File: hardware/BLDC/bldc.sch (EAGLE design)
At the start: 87 parts, among them J1 PWR_2_XT30PW-M, J2 LINEAR_3_JST_PH_RA, J3 LINEAR_8_JST_PH_RA, U1 MA702, U10 MCP2542FD, U11 LDFM33PUR, U2 DRV8323RS, U3 TPN7R006PL, U4 TPN7R006PL, U5 TPN7R006PL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

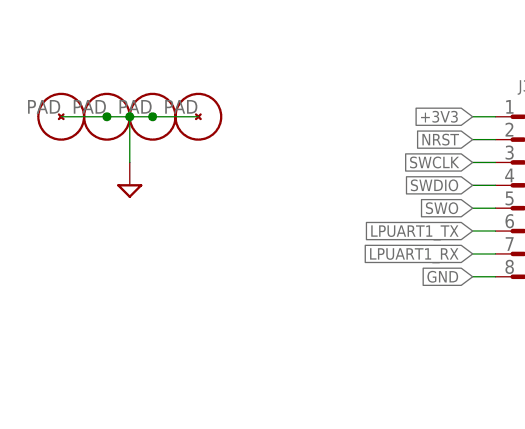
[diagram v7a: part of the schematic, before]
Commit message: Eagle board thickness
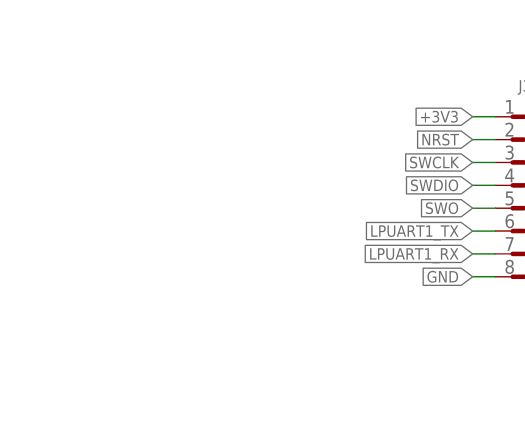
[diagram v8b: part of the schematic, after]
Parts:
- removed H1, H2, H3, H4: PCB_MOUNT_HOLE_M2, _T_conn:PCB_MOUNT_HOLE_M2
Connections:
- net GND: no longer H1.P1, H2.P1, H3.P1, H4.P1
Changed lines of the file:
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@@
 <schematic_group name="FDCAN"/>
 <schematic_group name="POWER_CONN"/>
-<schematic_group name="MOUNTING_HOLES"/>
 <schematic_group name="5V_3.3V_REG"/>
 <schematic_group name="LED_INFO"/>
@@
 <part name="U7" library="_T_transistors" library_urn="urn:adsk.eagle:library:19605452" deviceset="TPN7R006PL" device="" package3d_urn="urn:adsk.eagle:package:20292156/4"/>
 <part name="U8" library="_T_transistors" library_urn="urn:adsk.eagle:library:19605452" deviceset="TPN7R006PL" device="" package3d_urn="urn:adsk.eagle:package:20292156/4"/>
-<part name="H1" library="_T_conn" library_urn="urn:adsk.eagle:library:19570503" deviceset="PCB_MOUNT_HOLE" device="_M2" package3d_urn="urn:adsk.eagle:package:20293119/4"/>
-<part name="H2" library="_T_conn" library_urn="urn:adsk.eagle:library:19570503" deviceset="PCB_MOUNT_HOLE" device="_M2" package3d_urn="urn:adsk.eagle:package:20293119/4"/>
-<part name="H3" library="_T_conn" library_urn="urn:adsk.eagle:library:19570503" deviceset="PCB_MOUNT_HOLE" device="_M2" package3d_urn="urn:adsk.eagle:package:20293119/4"/>
-<part name="H4" library="_T_conn" library_urn="urn:adsk.eagle:library:19570503" deviceset="PCB_MOUNT_HOLE" device="_M2" package3d_urn="urn:adsk.eagle:package:20293119/4"/>
-<part name="GND2" library="_T_power" library_urn="urn:adsk.eagle:library:19572085" deviceset="GND" device=""/>
 <part name="U9" library="_T_ic" library_urn="urn:adsk.eagle:library:19571245" deviceset="STM32G4_UFQFPN48_T1" device="" package3d_urn="urn:adsk.eagle:package:19324073/6"/>
 <part name="L1" library="_T_rcl" library_urn="urn:adsk.eagle:library:19571919" deviceset="DC_CHOKE" device="_FERRITE_BEAD_0603" package3d_urn="urn:adsk.eagle:package:20293176/3" value="600R@100MHz"/>
@@
 <attribute name="NAME" x="250.19" y="90.17" size="1.27" layer="95" rot="MR180"/>
 </instance>
-<instance part="H1" gate="G$1" x="-83.82" y="175.26" smashed="yes" grouprefs="MOUNTING_HOLES"/>
-<instance part="H2" gate="G$1" x="-78.74" y="175.26" smashed="yes" grouprefs="MOUNTING_HOLES"/>
-<instance part="H3" gate="G$1" x="-73.66" y="175.26" smashed="yes" grouprefs="MOUNTING_HOLES"/>
-<instance part="H4" gate="G$1" x="-68.58" y="175.26" smashed="yes" grouprefs="MOUNTING_HOLES"/>
-<instance part="GND2" gate="G$1" x="-76.2" y="167.64" smashed="yes" grouprefs="MOUNTING_HOLES"/>
 <instance part="U9" gate="A" x="-35.56" y="91.44" smashed="yes" grouprefs="UC_STM32G4">
 <attribute name="NAME" x="-55.5244" y="133.5786" size="1.27" layer="95" ratio="6" rot="SR0"/>
@@
 </segment>
 <segment>
-<pinref part="H1" gate="G$1" pin="P1"/>
-<pinref part="H2" gate="G$1" pin="P1"/>
-<wire x1="-83.82" y1="175.26" x2="-78.74" y2="175.26" width="0.1524" layer="91" grouprefs="MOUNTING_HOLES"/>
-<pinref part="H3" gate="G$1" pin="P1"/>
-<wire x1="-78.74" y1="175.26" x2="-76.2" y2="175.26" width="0.1524" layer="91" grouprefs="MOUNTING_HOLES"/>
-<junction x="-78.74" y="175.26" grouprefs="MOUNTING_HOLES"/>
-<pinref part="H4" gate="G$1" pin="P1"/>
-<wire x1="-76.2" y1="175.26" x2="-73.66" y2="175.26" width="0.1524" layer="91" grouprefs="MOUNTING_HOLES"/>
-<wire x1="-73.66" y1="175.26" x2="-68.58" y2="175.26" width="0.1524" layer="91" grouprefs="MOUNTING_HOLES"/>
-<junction x="-73.66" y="175.26" grouprefs="MOUNTING_HOLES"/>
-<pinref part="GND2" gate="G$1" pin="GND"/>
-<wire x1="-76.2" y1="170.18" x2="-76.2" y2="175.26" width="0.1524" layer="91" grouprefs="MOUNTING_HOLES"/>
-<junction x="-76.2" y="175.26" grouprefs="MOUNTING_HOLES"/>
-</segment>
-<segment>
